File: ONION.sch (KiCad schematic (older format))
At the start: 13 parts, among them J5 Conn_02x06, U7 Omega2+, U8 FSM1LPTR

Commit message: diseño de esquematico
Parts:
- C44: renamed from C42; value 0.1uF -> 1uF
- U8: footprint SWITCH_FSM1LPA -> library:FSM1LPTR
- renumbered C43 to C45, C44 to C46, D14 to D8, R9 to R12, R10 to R13, R11 to R14, R12 to R15, R14 to R16
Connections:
- net labels removed: I2C_00, I2C_01, I2C_0[0..1], JTAG0, JTAG1, JTAG2, JTAG3, JTAG4, JTAG5, JTAG[0..5], on_3v3
- wire segments 88 -> 74
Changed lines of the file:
@@
 $EndDescr
 $Comp
-L power:GND #PWR0143
+L power:GND #PWR052
 U 1 1 5D428107
 P 5000 4800
-F 0 "#PWR0143" H 5000 4550 50  0001 C CNN
+F 0 "#PWR052" H 5000 4550 50  0001 C CNN
 F 1 "GND" H 5005 4627 50  0000 C CNN
 F 2 "" H 5000 4800 50  0001 C CNN
@@
 Wire Wire Line
 	3950 4200 3850 4200
-Text HLabel 3500 1450 0    50   Input ~ 0
-on_3v3
 Wire Wire Line
 	3900 1500 3900 1550
@@
 P 4350 1700
 AR Path="/5CD05F2F/5D451473" Ref="C?"  Part="0"
-AR Path="/5D3DE78E/5D451473" Ref="C43"  Part="1"
-F 0 "C43" H 4465 1746 50  0000 L CNN
+AR Path="/5D3DE78E/5D451473" Ref="C45"  Part="1"
+F 0 "C45" H 4465 1746 50  0000 L CNN
 F 1 "0.1uF" H 4465 1655 50  0000 L CNN
 F 2 "Capacitor_SMD:C_0603_1608Metric_Pad1.05x0.95mm_HandSolder" H 4388 1550 50  0001 C CNN
@@
 	4350 1500 3900 1500
 Wire Wire Line
-	3500 1450 3600 1450
-Wire Wire Line
 	3900 1450 3900 1500
 Connection ~ 3900 1500
@@
 	4350 2000 4100 2000
 $Comp
-L power:GND #PWR0144
+L power:GND #PWR051
 U 1 1 5D454107
 P 4100 2050
-F 0 "#PWR0144" H 4100 1800 50  0001 C CNN
+F 0 "#PWR051" H 4100 1800 50  0001 C CNN
 F 1 "GND" H 4105 1877 50  0000 C CNN
 F 2 "" H 4100 2050 50  0001 C CNN
@@
 P 3900 1700
 AR Path="/5CD05F2F/5D44FAD3" Ref="C?"  Part="0"
-AR Path="/5D3DE78E/5D44FAD3" Ref="C42"  Part="1"
-F 0 "C42" H 4015 1746 50  0000 L CNN
-F 1 "0.1uF" H 4015 1655 50  0000 L CNN
+AR Path="/5D3DE78E/5D44FAD3" Ref="C44"  Part="1"
+F 0 "C44" H 4015 1746 50  0000 L CNN
+F 1 "1uF" H 4015 1655 50  0000 L CNN
 F 2 "Capacitor_SMD:C_0603_1608Metric_Pad1.05x0.95mm_HandSolder" H 3938 1550 50  0001 C CNN
 F 3 "" H 3900 1700 50  0001 C CNN
@@
 RST_BTN
 $Comp
-L BAT2032:R R9
+L BAT2032:R R12
 U 1 1 5CD91C3B
 P 3850 3050
-F 0 "R9" V 3800 3250 50  0000 C CNN
+F 0 "R12" V 3800 3250 50  0000 C CNN
 F 1 "100" V 3850 3050 50  0000 C CNN
 F 2 "Resistor_SMD:R_0603_1608Metric_Pad1.05x0.95mm_HandSolder" V 3780 3050 50  0001 C CNN
@@
 $EndComp
 $Comp
-L BAT2032:R R10
+L BAT2032:R R13
 U 1 1 5CD95E75
 P 3850 3150
-F 0 "R10" V 3800 3350 50  0000 C CNN
+F 0 "R13" V 3800 3350 50  0000 C CNN
 F 1 "100" V 3850 3150 50  0000 C CNN
 F 2 "Resistor_SMD:R_0603_1608Metric_Pad1.05x0.95mm_HandSolder" V 3780 3150 50  0001 C CNN
@@
 $EndComp
 $Comp
-L BAT2032:R R11
+L BAT2032:R R14
 U 1 1 5CD970C9
 P 3850 3250
-F 0 "R11" V 3800 3450 50  0000 C CNN
+F 0 "R14" V 3800 3450 50  0000 C CNN
 F 1 "100" V 3850 3250 50  0000 C CNN
 F 2 "Resistor_SMD:R_0603_1608Metric_Pad1.05x0.95mm_HandSolder" V 3780 3250 50  0001 C CNN
@@
 $EndComp
 $Comp
-L BAT2032:R R12
+L BAT2032:R R15
 U 1 1 5CD983F0
 P 3850 3350
-F 0 "R12" V 3800 3550 50  0000 C CNN
+F 0 "R15" V 3800 3550 50  0000 C CNN
 F 1 "100" V 3850 3350 50  0000 C CNN
 F 2 "Resistor_SMD:R_0603_1608Metric_Pad1.05x0.95mm_HandSolder" V 3780 3350 50  0001 C CNN
@@
 Text Label 3350 3350 0    50   ~ 0
 SPI_CS
-Text HLabel 4100 2700 0    50   Output ~ 0
-BOOT0
-$Comp
-L power:GND #PWR0145
+$Comp
+L power:GND #PWR053
 U 1 1 5CD47976
 P 6650 2700
-F 0 "#PWR0145" H 6650 2450 50  0001 C CNN
+F 0 "#PWR053" H 6650 2450 50  0001 C CNN
 F 1 "GND" V 6655 2572 50  0000 R CNN
 F 2 "" H 6650 2700 50  0001 C CNN
@@
 	1    0    0    -1
 $EndComp
-Text HLabel 5600 1500 0    50   Input ~ 0
-on_3v3
 NoConn ~ 4300 3850
 Text Label 7450 1500 0    50   ~ 0
@@
 	7300 2050 7300 1800
 $Comp
-L power:GND #PWR0146
+L power:GND #PWR054
 U 1 1 5CD5D462
 P 7300 2050
-F 0 "#PWR0146" H 7300 1800 50  0001 C CNN
+F 0 "#PWR054" H 7300 1800 50  0001 C CNN
 F 1 "GND" V 7305 1922 50  0000 R CNN
 F 2 "" H 7300 2050 50  0001 C CNN
@@
 P 7300 1650
 AR Path="/5CD05F2F/5CD5AB36" Ref="C?"  Part="0"
-AR Path="/5D3DE78E/5CD5AB36" Ref="C44"  Part="1"
-F 0 "C44" H 7415 1696 50  0000 L CNN
+AR Path="/5D3DE78E/5CD5AB36" Ref="C46"  Part="1"
+F 0 "C46" H 7415 1696 50  0000 L CNN
 F 1 "0.1uF" H 7415 1605 50  0000 L CNN
 F 2 "Capacitor_SMD:C_0603_1608Metric_Pad1.05x0.95mm_HandSolder" H 7338 1500 50  0001 C CNN
@@
 $EndComp
 $Comp
-L BAT2032:R R14
+L BAT2032:R R16
 U 1 1 5CD54029
 P 6150 1500
-F 0 "R14" V 6100 1700 50  0000 C CNN
+F 0 "R16" V 6100 1700 50  0000 C CNN
 F 1 "10K" V 6150 1500 50  0000 C CNN
 F 2 "Resistor_SMD:R_0603_1608Metric_Pad1.05x0.95mm_HandSolder" V 6080 1500 50  0001 C CNN
@@
 $EndComp
 Wire Wire Line
-	5600 1500 5800 1500
-Wire Wire Line
 	6650 2700 6650 2450
 Wire Wire Line
@@
 F 0 "U8" H 6725 2307 60  0000 C CNN
 F 1 "FSM1LPTR" H 6725 2201 60  0000 C CNN
-F 2 "SWITCH_FSM1LPA" H 6700 2150 60  0001 C CNN
+F 2 "library:FSM1LPTR" H 6700 2150 60  0001 C CNN
 F 3 "" H 6300 2000 60  0000 C CNN
 F 4 "450-1756-1-ND" H 6700 2000 50  0001 C CNN "digikey"
@@
 	0    1    1    0
 $EndComp
-Text Label 2050 6300 0    50   ~ 0
-NRST
-Text Label 2050 6100 0    50   ~ 0
-TRST
-Text Label 2050 5900 0    50   ~ 0
-TDO
-Text Label 2050 5700 0    50   ~ 0
-TDI
-Text Label 2050 5500 0    50   ~ 0
-TCK
-Text Label 2050 5300 0    50   ~ 0
-TMS
-Text Label 1700 6300 0    50   ~ 0
-JTAG5
-Text Label 1700 6100 0    50   ~ 0
-JTAG4
-Text Label 1700 5900 0    50   ~ 0
-JTAG3
-Text Label 1700 5700 0    50   ~ 0
-JTAG2
-Text Label 1700 5500 0    50   ~ 0
-JTAG1
-Text Label 1700 5300 0    50   ~ 0
-JTAG0
-Wire Wire Line
-	1650 6300 2350 6300
-Wire Wire Line
-	1650 6100 2350 6100
-Wire Wire Line
-	1650 5900 2350 5900
-Wire Wire Line
-	1650 5700 2350 5700
-Wire Wire Line
-	1650 5500 2350 5500
-Wire Wire Line
-	1650 5300 2350 5300
-Entry Wire Line
-	1550 6200 1650 6300
-Entry Wire Line
-	1550 6000 1650 6100
-Entry Wire Line
-	1550 5800 1650 5900
-Entry Wire Line
-	1550 5600 1650 5700
-Entry Wire Line
-	1550 5400 1650 5500
-Entry Wire Line
-	1550 5200 1650 5300
-Wire Bus Line
-	1200 5100 1550 5100
-Text HLabel 3850 3650 0    50   Input ~ 0
-JTDO_OMEGA
-Text GLabel 4100 2800 0    50   Input ~ 0
+Text GLabel 4100 2750 0    50   Input ~ 0
 BOOT0
-Wire Wire Line
-	4200 2700 4100 2700
-Wire Wire Line
-	4100 2800 4200 2800
-Wire Bus Line
-	6300 4850 6650 4850
-Entry Wire Line
-	6650 4950 6750 5050
-Entry Wire Line
-	6650 5150 6750 5250
-Wire Wire Line
-	6750 5050 7450 5050
-Wire Wire Line
-	6750 5250 7450 5250
-Text Label 6750 5050 0    50   ~ 0
-I2C_00
-Text Label 6750 5250 0    50   ~ 0
-I2C_01
-Text Label 7150 5050 0    50   ~ 0
-I2C_SCL
-Text Label 7150 5250 0    50   ~ 0
-I2C_SDA
-Text GLabel 6300 4850 0    50   Input ~ 0
-I2C_0[0..1]
-Text GLabel 1200 5100 0    50   Input ~ 0
-JTAG[0..5]
-Text HLabel 3850 3550 0    50   Output ~ 0
-JTCK
-Text HLabel 3800 2650 0    50   Output ~ 0
-JNRST
-Text HLabel 3800 2550 0    50   Output ~ 0
-JTRST
-Text HLabel 3800 2350 0    50   Output ~ 0
-JTMS
-Text HLabel 3800 2450 0    50   Output ~ 0
-JTDO
 Text GLabel 6200 3350 2    50   Output ~ 0
 USART_TX
@@
 USART_RX
 NoConn ~ 5700 2550
-Wire Wire Line
-	4300 2750 4200 2750
-Wire Wire Line
-	4200 2750 4200 2700
-Wire Wire Line
-	4200 2800 4200 2750
-Connection ~ 4200 2750
 $Comp
 L Connector_Generic:Conn_02x06_Counter_Clockwise J?
@@
 	3550 1300 3600 1300
 Wire Wire Line
-	3600 1300 3600 1450
-Connection ~ 3600 1450
-Wire Wire Line
-	3600 1450 3900 1450
-Wire Wire Line
 	5700 1300 5800 1300
 Wire Wire Line
 	5800 1300 5800 1500
-Connection ~ 5800 1500
 Wire Wire Line
 	5800 1500 6000 1500
@@
 	1950 1900 1950 2100
 $Comp
-L power:GND #PWR0158
+L power:GND #PWR049
 U 1 1 5E11F7EF
 P 2500 2100
-F 0 "#PWR0158" H 2500 1850 50  0001 C CNN
+F 0 "#PWR049" H 2500 1850 50  0001 C CNN
 F 1 "GND" V 2505 1972 50  0000 R CNN
 F 2 "" H 2500 2100 50  0001 C CNN
@@
 $EndComp
 $Comp
-L power:GND #PWR0159
+L power:GND #PWR050
 U 1 1 5E1233E4
 P 2500 2600
-F 0 "#PWR0159" H 2500 2350 50  0001 C CNN
+F 0 "#PWR050" H 2500 2350 50  0001 C CNN
 F 1 "GND" V 2505 2472 50  0000 R CNN
 F 2 "" H 2500 2600 50  0001 C CNN
@@
 P 1900 2600
 AR Path="/5CD17BDC/5E133FCC" Ref="#PWR?"  Part="1"
-AR Path="/5D3DE78E/5E133FCC" Ref="#PWR0214"  Part="1"
-F 0 "#PWR0214" H 1900 2450 50  0001 C CNN
+AR Path="/5D3DE78E/5E133FCC" Ref="#PWR048"  Part="1"
+F 0 "#PWR048" H 1900 2450 50  0001 C CNN
 F 1 "+5VD" H 1900 2750 50  0000 C CNN
 F 2 "" H 1900 2600 50  0001 C CNN
@@
 P 8100 3150
 AR Path="/5CD17BDC/5E14B66F" Ref="D?"  Part="1"
-AR Path="/5D3DE78E/5E14B66F" Ref="D14"  Part="1"
-F 0 "D14" V 8139 3033 50  0000 R CNN
+AR Path="/5D3DE78E/5E14B66F" Ref="D8"  Part="1"
+F 0 "D8" V 8139 3033 50  0000 R CNN
 F 1 "LED" V 8048 3033 50  0000 R CNN
 F 2 "LED_SMD:LED_0603_1608Metric_Pad1.05x0.95mm_HandSolder" H 8100 3150 50  0001 C CNN
@@
 P 8100 3850
 AR Path="/5CD17BDC/5E14B67C" Ref="#PWR?"  Part="1"
-AR Path="/5D3DE78E/5E14B67C" Ref="#PWR0227"  Part="1"
-F 0 "#PWR0227" H 8100 3600 50  0001 C CNN
+AR Path="/5D3DE78E/5E14B67C" Ref="#PWR055"  Part="1"
+F 0 "#PWR055" H 8100 3600 50  0001 C CNN
 F 1 "GND" H 8105 3677 50  0000 C CNN
 F 2 "" H 8100 3850 50  0001 C CNN
@@
 RED
 NoConn ~ 4300 3750
-Wire Bus Line
-	6650 4850 6650 5150
-Wire Bus Line
-	1550 5100 1550 6200
+Text GLabel 3800 2350 0    50   Output ~ 0
+JTMS
+Text GLabel 3850 3650 0    50   Output ~ 0
+JTDO
+Text GLabel 3800 2550 0    50   Output ~ 0
+JTRST
+Text GLabel 3800 2650 0    50   Output ~ 0
+JNRST
+Wire Wire Line
+	4100 2750 4300 2750
+Text GLabel 3850 3550 0    50   Output ~ 0
+JTCK
+Text GLabel 3800 2450 0    50   Input ~ 0
+JTDO_OMEGA
+Text GLabel 6200 4050 2    50   Input ~ 0
+I2C_SCL
+Text GLabel 6200 4150 2    50   Input ~ 0
+I2C_SDA
+Wire Wire Line
+	3600 1450 3900 1450
+Wire Wire Line
+	3600 1300 3600 1450
 $EndSCHEMATC

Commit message: diseño de esquematico CASI FINAL
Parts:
- J5: symbol Connector_Generic:Conn_02x06_Counter_Clockwise -> Connector_Generic:Conn_02x06_Odd_Even
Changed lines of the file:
@@
-EESchema Schematic File Version 4
+EESchema Schematic File Version 5
 LIBS:power-cache
 EELAYER 29 0
@@
 NoConn ~ 5700 2550
 $Comp
-L Connector_Generic:Conn_02x06_Counter_Clockwise J?
+L Connector_Generic:Conn_02x06_Odd_Even J?
 U 1 1 5E0A8FB7
 P 2150 2300
@@
 Wire Wire Line
 	1450 2300 1950 2300
+Text Label 1600 2300 0    50   ~ 0
+I2C_SCL
 Text Label 1600 2200 0    50   ~ 0
-I2C_SCL
-Text Label 1600 2300 0    50   ~ 0
 I2C_SDA
 Wire Wire Line

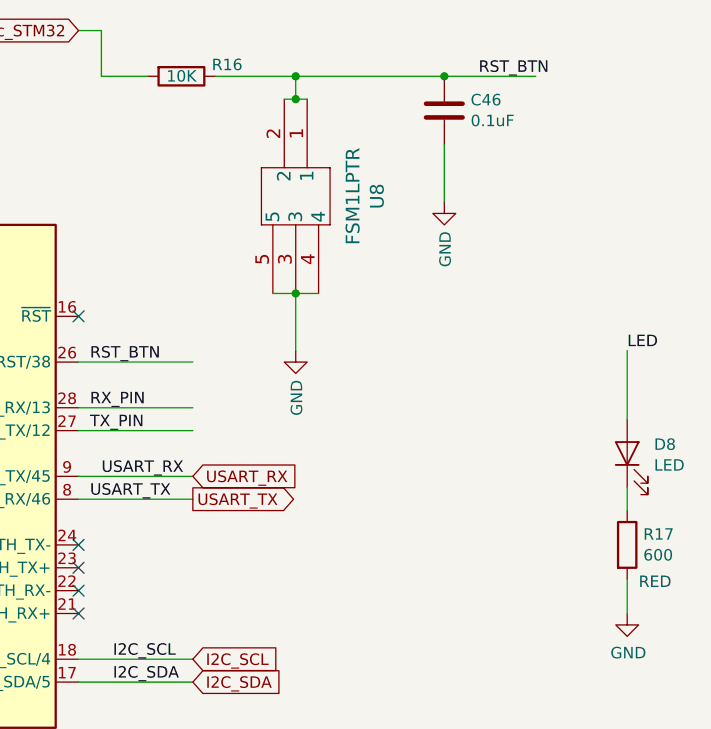
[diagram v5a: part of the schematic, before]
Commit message: programacion luego del diseño del embebido
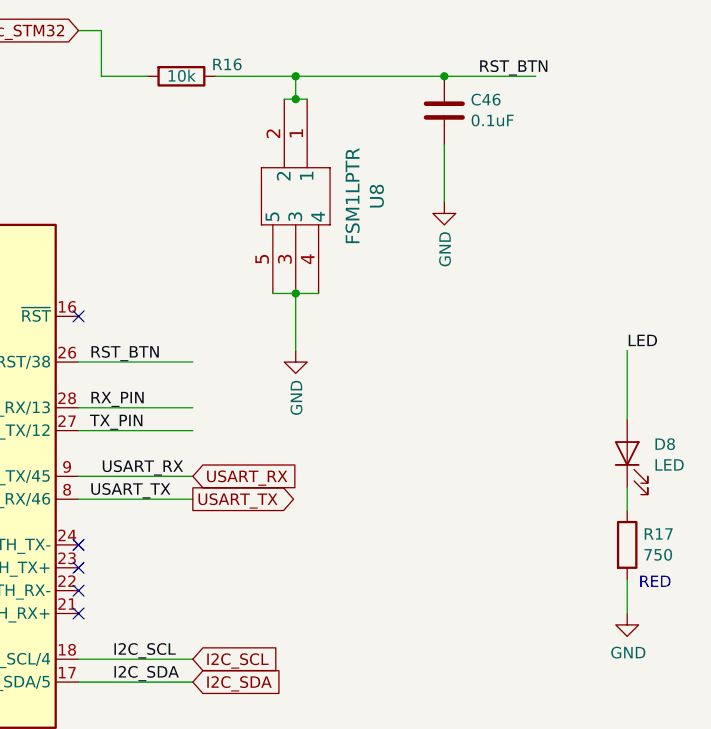
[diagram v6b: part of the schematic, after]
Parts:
- R16: value 10K -> 10k
- R17: value 600 -> 750
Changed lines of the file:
@@
 P 6150 1500
 F 0 "R16" V 6100 1700 50  0000 C CNN
-F 1 "10K" V 6150 1500 50  0000 C CNN
+F 1 "10k" V 6150 1500 50  0000 C CNN
 F 2 "Resistor_SMD:R_0603_1608Metric_Pad1.05x0.95mm_HandSolder" V 6080 1500 50  0001 C CNN
 F 3 "~" H 6150 1500 50  0001 C CNN
@@
 AR Path="/5D3DE78E/5E14B676" Ref="R17"  Part="1"
 F 0 "R17" H 8170 3596 50  0000 L CNN
-F 1 "600" H 8170 3505 50  0000 L CNN
+F 1 "750" H 8170 3505 50  0000 L CNN
 F 2 "Resistor_SMD:R_0603_1608Metric_Pad1.05x0.95mm_HandSolder" V 8030 3550 50  0001 C CNN
 F 3 "~" H 8100 3550 50  0001 C CNN
-F 4 "" H 8100 3550 50  0001 C CNN "Digikey"
 	1    8100 3550
 	1    0    0    -1
